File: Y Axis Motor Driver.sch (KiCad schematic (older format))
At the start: 37 parts, among them J1 Motor Y, U1 TMC2209-LA

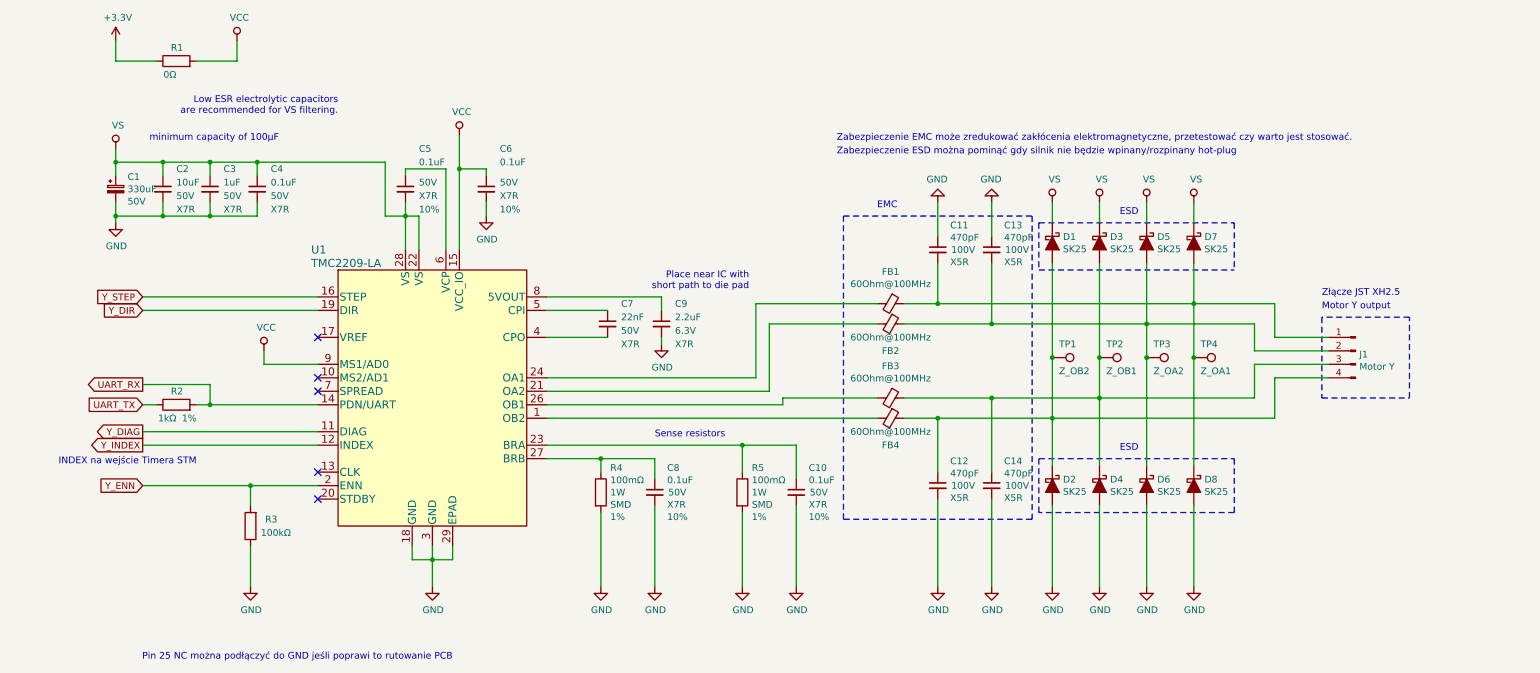
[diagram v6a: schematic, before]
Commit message: Added analog input
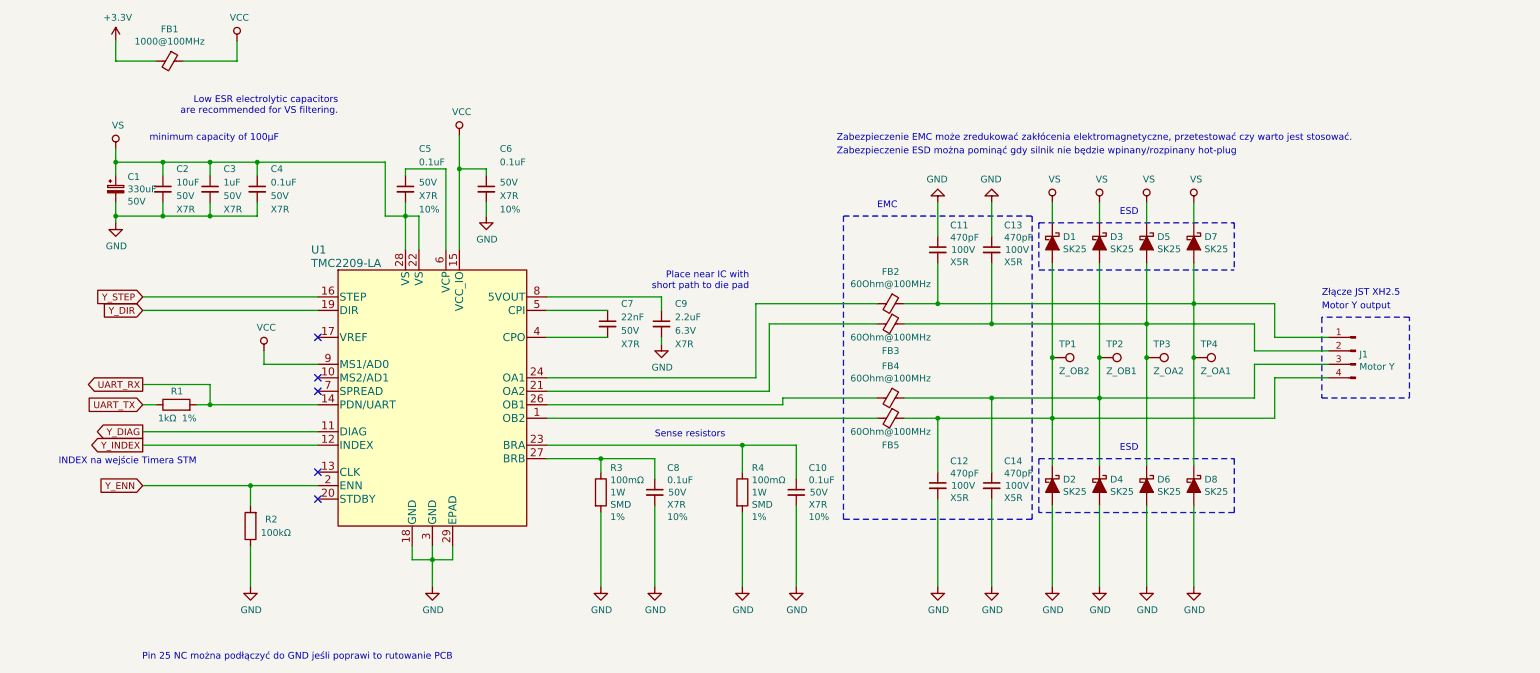
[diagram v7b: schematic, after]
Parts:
- removed R1: 0Ω, Resistor_SMD:R_0805_2012Metric, symbol Device:R
- added FB1: 1000@100MHz, Inductor_SMD:L_0805_2012Metric, symbol Device:Ferrite_Bead_Small
- renumbered FB1 to FB2, FB2 to FB3, FB3 to FB4, FB4 to FB5, R2 to R1, R3 to R2, R4 to R3, R5 to R4
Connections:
- net +3V3: now also FB1.2
- net VCC: now also FB1.1
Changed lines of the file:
@@
 P 5000 4450
 AR Path="/5DE588DC/5E249033" Ref="R?"  Part="1"
-AR Path="/5DE587B9/5E249033" Ref="R4"  Part="1"
-F 0 "R4" H 5070 4632 50  0000 L CNN
+AR Path="/5DE587B9/5E249033" Ref="R3"  Part="1"
+F 0 "R3" H 5070 4632 50  0000 L CNN
 F 1 "100mΩ" H 5070 4541 50  0000 L CNN
 F 2 "Resistor_SMD:R_2010_5025Metric" V 4930 4450 50  0001 C CNN
@@
 P 6050 4450
 AR Path="/5DE588DC/5E24905B" Ref="R?"  Part="1"
-AR Path="/5DE587B9/5E24905B" Ref="R5"  Part="1"
-F 0 "R5" H 6120 4632 50  0000 L CNN
+AR Path="/5DE587B9/5E24905B" Ref="R4"  Part="1"
+F 0 "R4" H 6120 4632 50  0000 L CNN
 F 1 "100mΩ" H 6120 4541 50  0000 L CNN
 F 2 "Resistor_SMD:R_2010_5025Metric" V 5980 4450 50  0001 C CNN
@@
 P 7150 3050
 AR Path="/5DE588DC/5E2490C7" Ref="FB?"  Part="1"
-AR Path="/5DE587B9/5E2490C7" Ref="FB1"  Part="1"
-F 0 "FB1" V 6913 3050 50  0000 C CNN
+AR Path="/5DE587B9/5E2490C7" Ref="FB2"  Part="1"
+F 0 "FB2" V 6913 3050 50  0000 C CNN
 F 1 "60Ohm@100MHz" V 7004 3050 50  0000 C CNN
 F 2 "Inductor_SMD:L_0805_2012Metric" V 7080 3050 50  0001 C CNN
@@
 P 7150 3200
 AR Path="/5DE588DC/5E2490CE" Ref="FB?"  Part="1"
-AR Path="/5DE587B9/5E2490CE" Ref="FB2"  Part="1"
-F 0 "FB2" V 7350 3200 50  0000 C CNN
+AR Path="/5DE587B9/5E2490CE" Ref="FB3"  Part="1"
+F 0 "FB3" V 7350 3200 50  0000 C CNN
 F 1 "60Ohm@100MHz" V 7250 3200 50  0000 C CNN
 F 2 "Inductor_SMD:L_0805_2012Metric" V 7080 3200 50  0001 C CNN
@@
 P 7150 3750
 AR Path="/5DE588DC/5E2490D5" Ref="FB?"  Part="1"
-AR Path="/5DE587B9/5E2490D5" Ref="FB3"  Part="1"
-F 0 "FB3" V 6913 3750 50  0000 C CNN
+AR Path="/5DE587B9/5E2490D5" Ref="FB4"  Part="1"
+F 0 "FB4" V 6913 3750 50  0000 C CNN
 F 1 "60Ohm@100MHz" V 7004 3750 50  0000 C CNN
 F 2 "Inductor_SMD:L_0805_2012Metric" V 7080 3750 50  0001 C CNN
@@
 P 7150 3900
 AR Path="/5DE588DC/5E2490DC" Ref="FB?"  Part="1"
-AR Path="/5DE587B9/5E2490DC" Ref="FB4"  Part="1"
-F 0 "FB4" V 7350 3900 50  0000 C CNN
+AR Path="/5DE587B9/5E2490DC" Ref="FB5"  Part="1"
+F 0 "FB5" V 7350 3900 50  0000 C CNN
 F 1 "60Ohm@100MHz" V 7250 3900 50  0000 C CNN
 F 2 "Inductor_SMD:L_0805_2012Metric" V 7080 3900 50  0001 C CNN
@@
 P 2400 4700
 AR Path="/5DE588DC/5E249277" Ref="R?"  Part="1"
-AR Path="/5DE587B9/5E249277" Ref="R3"  Part="1"
-F 0 "R3" H 2200 4650 50  0000 L CNN
+AR Path="/5DE587B9/5E249277" Ref="R2"  Part="1"
+F 0 "R2" H 2200 4650 50  0000 L CNN
 F 1 "100kΩ" H 2100 4750 50  0000 L CNN
 F 2 "Resistor_SMD:R_0603_1608Metric" V 2330 4700 50  0001 C CNN
@@
 	1400 1250 1700 1250
 Wire Wire Line
-	2000 1250 2300 1250
+	1900 1250 2300 1250
 Wire Wire Line
 	2300 1250 2300 1100
@@
 P 1850 3800
 AR Path="/5DE588DC/5E249179" Ref="R?"  Part="1"
-AR Path="/5DE587B9/5E249179" Ref="R2"  Part="1"
-F 0 "R2" V 1950 3750 50  0000 L CNN
+AR Path="/5DE587B9/5E249179" Ref="R1"  Part="1"
+F 0 "R1" V 1950 3750 50  0000 L CNN
 F 1 "1kΩ" V 1750 3800 50  0000 L CNN
 F 2 "Resistor_SMD:R_0603_1608Metric" V 1780 3800 50  0001 C CNN
@@
 $EndComp
 $Comp
-L Device:R R?
-U 1 1 5E2C4255
-P 1850 1250
-AR Path="/5DE588DC/5E2C4255" Ref="R?"  Part="1"
-AR Path="/5DE587B9/5E2C4255" Ref="R1"  Part="1"
-F 0 "R1" V 1950 1200 50  0000 L CNN
-F 1 "0Ω" V 1750 1250 50  0000 L CNN
-F 2 "Resistor_SMD:R_0805_2012Metric" V 1780 1250 50  0001 C CNN
-F 3 "~" H 1850 1250 50  0001 C CNN
-F 4 "1%" V 1750 1100 50  0001 L CNN "Tolerancja"
-F 5 "" H 1850 1250 50  0001 C CNN "Model"
-F 6 "0.04651" H 1850 1250 50  0001 C CNN "Cena"
-F 7 "SMD" H 1850 1250 50  0001 C CNN "Typ"
-	1    1850 1250
-	0    -1   -1   0
+L Device:Ferrite_Bead_Small FB?
+U 1 1 5E5425BC
+P 1800 1250
+AR Path="/5DFB2EC0/5E5425BC" Ref="FB?"  Part="1"
+AR Path="/5DE587B9/5E5425BC" Ref="FB1"  Part="1"
+F 0 "FB1" V 1563 1250 50  0000 C CNN
+F 1 "1000@100MHz" V 1654 1250 50  0000 C CNN
+F 2 "Inductor_SMD:L_0805_2012Metric" V 1730 1250 50  0001 C CNN
+F 3 "~" H 1800 1250 50  0001 C CNN
+F 4 "0.2794" H 1800 1250 50  0001 C CNN "Cena"
+F 5 "https://www.tme.eu/pl/details/blm21ag102sn1d/ferryty-koraliki/murata/" H 1800 1250 50  0001 C CNN "Link"
+F 6 "BLM21AG102SN1D" H 1800 1250 50  0001 C CNN "Model"
+F 7 "Ferryt: koralik; Imp.@ 100MHz: 1000Ω; Montaż: SMD; 0,5A; Obud: 0805" H 1800 1250 50  0001 C CNN "Opis"
+F 8 "MURATA" H 1800 1250 50  0001 C CNN "Producent"
+F 9 "SMD" H 1800 1250 50  0001 C CNN "Typ"
+	1    1800 1250
+	0    1    1    0
 $EndComp
 $EndSCHEMATC

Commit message: Improve ESD Protection for TMC2209, Fuses. Schematic ready v1
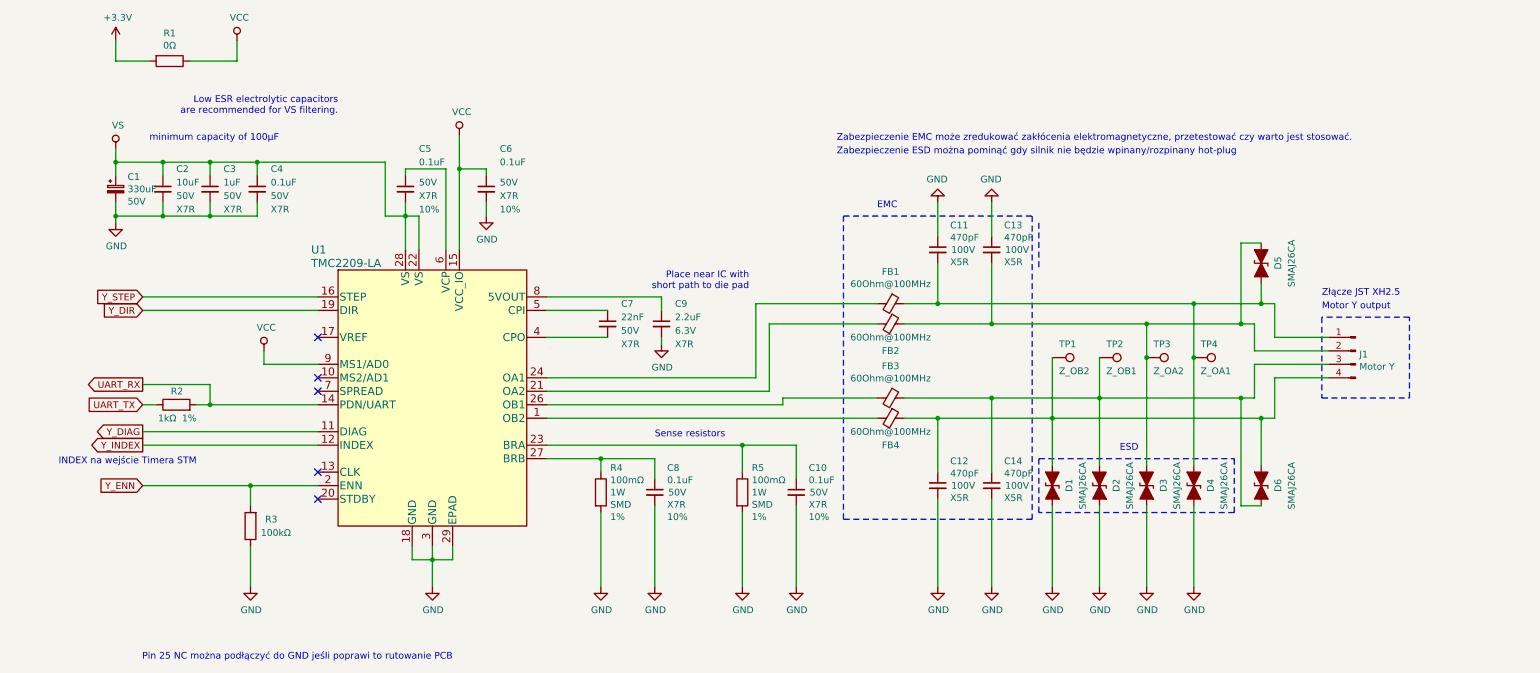
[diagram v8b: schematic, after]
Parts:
- removed D1, D2, D3, D4, D5, D6, D7, D8: SK25, Diode_SMD:D_SMB, symbol Device:D_Schottky_ALT
- removed FB1: 1000@100MHz, Inductor_SMD:L_0805_2012Metric, symbol Device:Ferrite_Bead_Small
- added D1, D2, D3, D4, D5, D6: SMAJ26CA, Diode_SMD:D_SMA, symbol Device:D_TVS_ALT
- added R1: 0Ω, symbol Device:R
- renumbered FB2 to FB1, FB3 to FB2, FB4 to FB3, FB5 to FB4, R1 to R2, R2 to R3, R3 to R4, R4 to R5
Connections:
- net +3V3: now also R1.2
- net GND: now also D1.2 (A2), D2.2 (A2), D3.2 (A2), D4.2 (A2)
- net VCC: now also R1.1
- net at C11.2, FB1.1, J1.1 (Pin_1)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: now also D4.1 (A1), D5.2 (A2)
- net at C13.2, FB2.1, J1.2 (Pin_2)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: now also D3.1 (A1), D5.1 (A1)
- net at C14.1, FB3.1, J1.3 (Pin_3)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: now also D2.1 (A1), D6.2 (A2)
- net at C12.1, FB4.1, J1.4 (Pin_4)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: now also D1.1 (A1), D6.1 (A1)
